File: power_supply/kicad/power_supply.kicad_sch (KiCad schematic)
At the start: 18 parts, among them J1 pcie_98, U1 URB2405YMD-10WR3, U2 ESD5344D

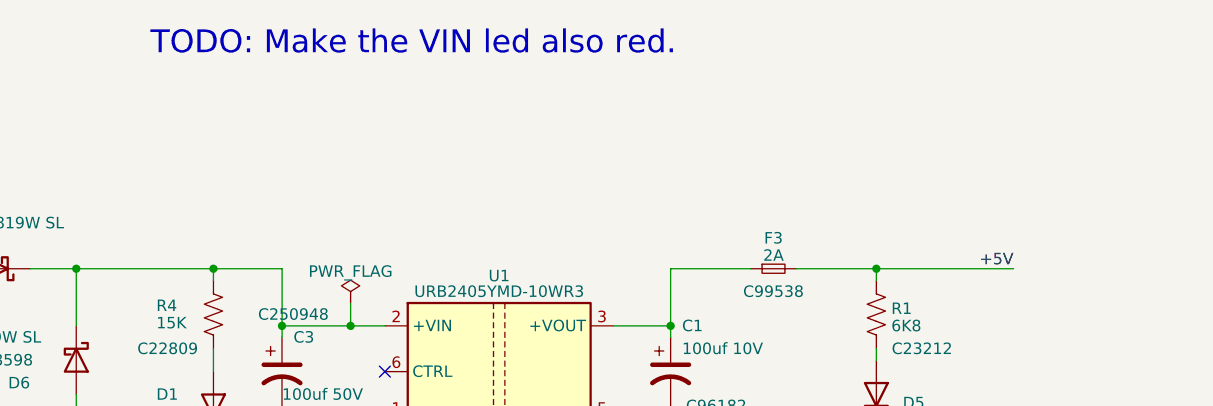
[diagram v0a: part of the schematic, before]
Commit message: Added TODOs to kicad schematics (adding a serial number silkscreen)
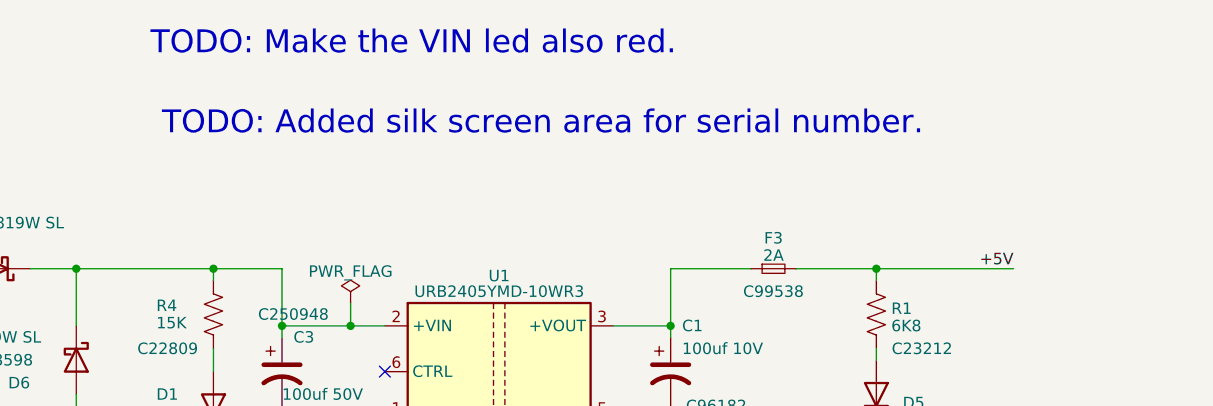
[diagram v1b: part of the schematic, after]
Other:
- note added: "TODO: Added silk screen area for serial number."
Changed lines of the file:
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@@
     (effects (font (size 3 3) (thickness 0.6) bold) (justify left bottom))
+  )
+  (text "TODO: Added silk screen area for serial number." (at 137.795 43.815 0)
+    (effects (font (size 2.54 2.54) (color 255 0 0 1)) (justify left bottom))
   )
   (label "VIN+" (at 95.25 58.42 0) (fields_autoplaced)
